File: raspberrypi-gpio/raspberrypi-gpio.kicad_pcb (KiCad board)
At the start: 2 copper layers, 85 x 56 mm, 1 part, among them P1 CONN_13X2

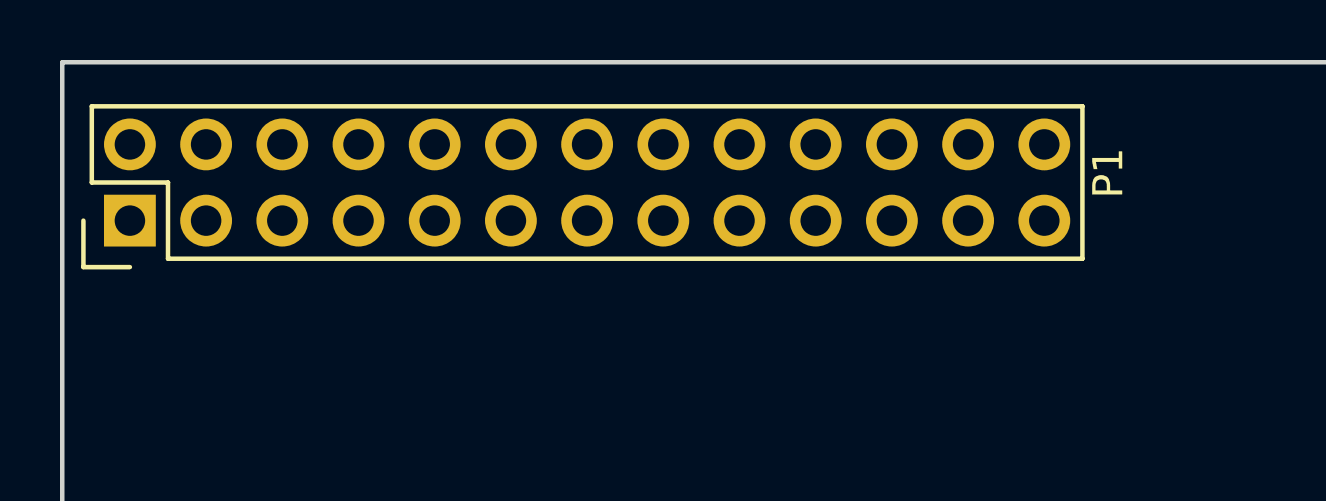
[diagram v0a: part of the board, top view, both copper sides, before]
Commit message: Remap respberrypi gpio template and use pin header fp from new lib.
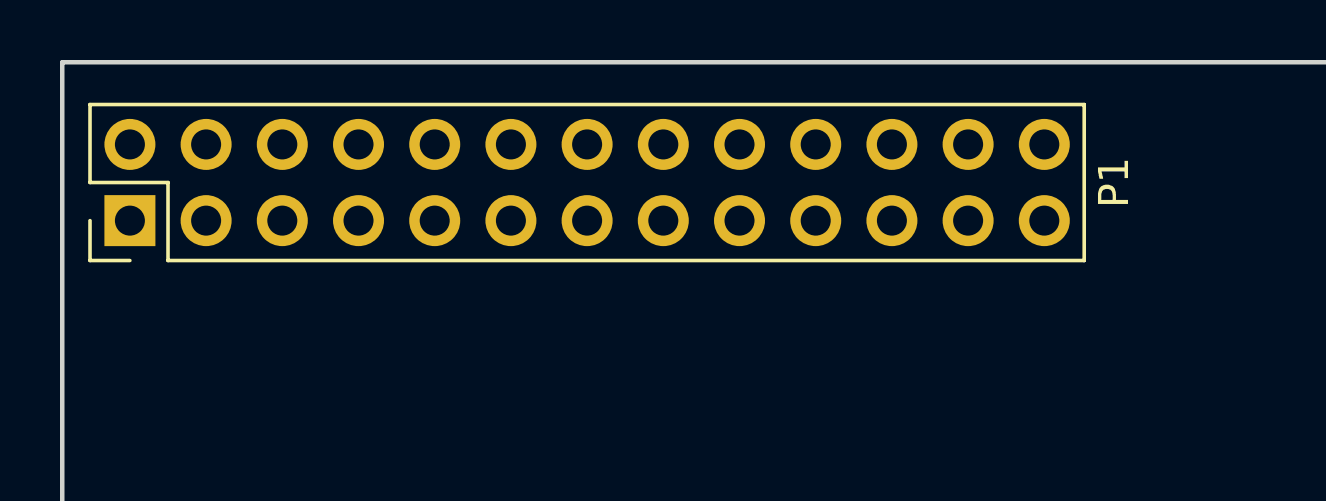
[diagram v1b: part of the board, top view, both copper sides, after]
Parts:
- P1: footprint Pin_Headers:Pin_Header_Straight_2x13 -> Connector_PinHeader_2.54mm:PinHeader_2x13_P2.54mm_Vertical
